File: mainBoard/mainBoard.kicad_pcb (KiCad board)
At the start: 4 copper layers, 110 x 75 mm, 74 parts, among them IC1 TCAN3414DR, J1 XT60PW-M, J10 RJ45, J11 RJ45, J12 Conn_01x03, J16 BM04B-SRSS-TB, J17 BM04B-SRSS-TB, J18 BM04B-SRSS-TB, J19 BM04B-SRSS-TB, J2 XT60PW-M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

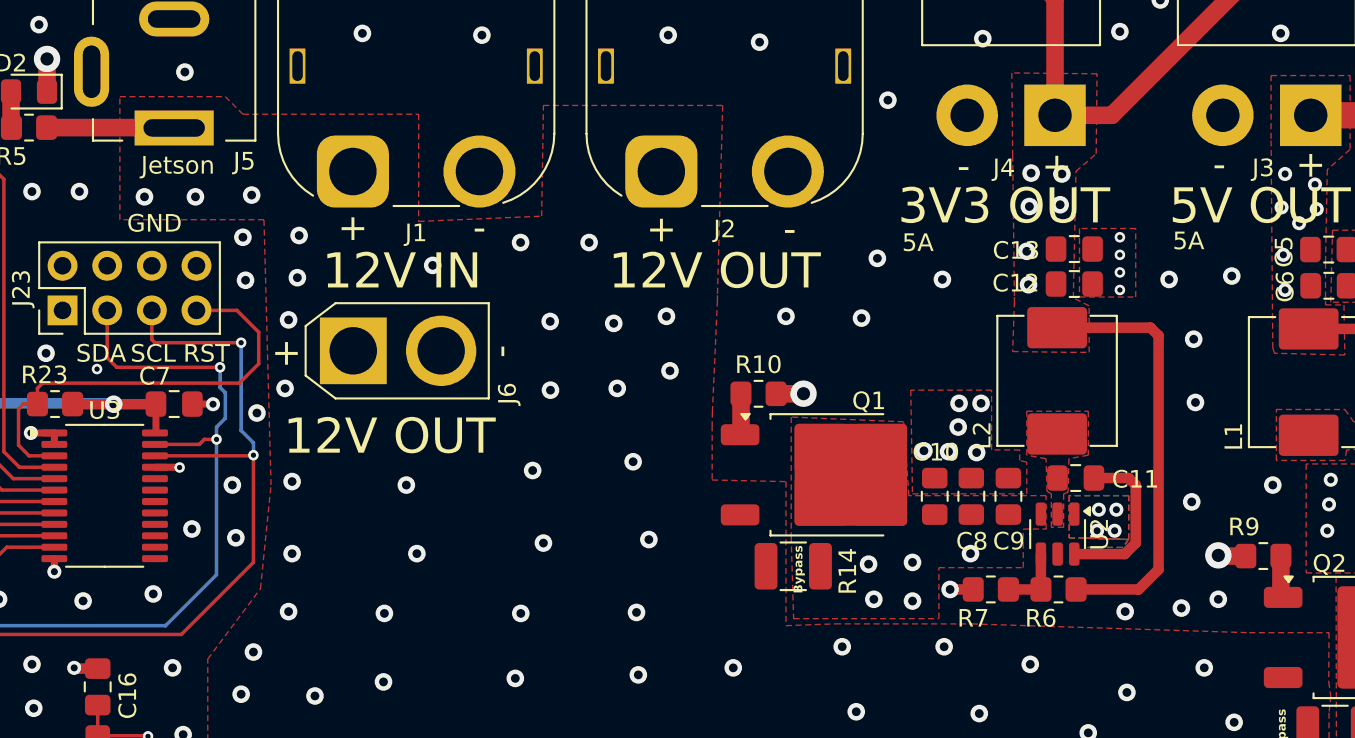
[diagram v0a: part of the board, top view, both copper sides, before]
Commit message: Fixed trace that had a unecessary via
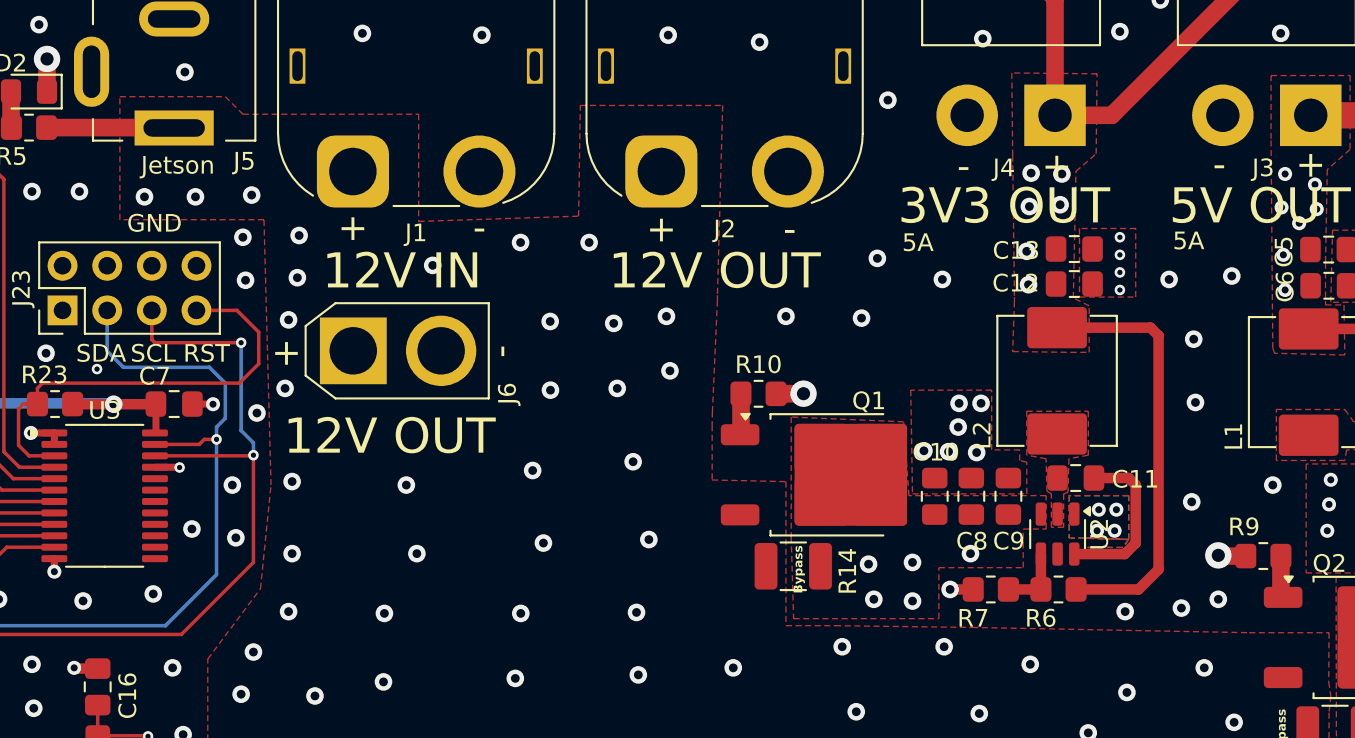
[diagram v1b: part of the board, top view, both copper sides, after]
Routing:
- net SDA1: track 54.6 -> 54.0 mm, vias 3 -> 2
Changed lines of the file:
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@@
 		(tags "resistor handsolder")
 		(property "Reference" "R13"
-			(at 1.1 -2.28 360)
+			(at 1.1 -2.28 0)
 			(layer "F.SilkS")
 			(effects
@@
 		)
 		(property "Value" "0"
-			(at 0 2.28 360)
+			(at 0 2.28 0)
 			(layer "F.Fab")
 			(hide yes)
@@
 		)
 		(fp_text user "${REFERENCE}"
-			(at 0 0 360)
+			(at 0 0 0)
 			(layer "F.Fab")
 			(effects
@@
 		(tags "resistor handsolder")
 		(property "Reference" "R9"
-			(at 1.1 1.65 360)
+			(at 1.1 1.65 0)
 			(layer "F.SilkS")
 			(effects
@@
 		)
 		(property "Value" "100"
-			(at 0 1.65 360)
+			(at 0 1.65 0)
 			(layer "F.Fab")
 			(hide yes)
@@
 		)
 		(fp_text user "${REFERENCE}"
-			(at 0 0 360)
+			(at 0 0 0)
 			(layer "F.Fab")
 			(effects
@@
 	)
 	(segment
-		(start 39.265 47.172643)
-		(end 39.265 44.475)
-		(width 0.2)
-		(layer "F.Cu")
-		(net 22)
-	)
-	(segment
 		(start 45.485786 51.814215)
 		(end 44.785786 51.814215)
@@
 	)
 	(segment
-		(start 45.685786 47.714215)
-		(end 39.806572 47.714215)
-		(width 0.2)
-		(layer "F.Cu")
-		(net 22)
-	)
-	(segment
 		(start 44.785786 51.814215)
 		(end 44.500001 52.1)
@@
 		(net 22)
 	)
-	(segment
-		(start 39.806572 47.714215)
-		(end 39.265 47.172643)
-		(width 0.2)
-		(layer "F.Cu")
-		(net 22)
-	)
 	(via
 		(at 23.385786 68.814215)
@@
 		(net 22)
 	)
-	(via
-		(at 45.685786 47.714215)
-		(size 0.6)
-		(drill 0.3)
-		(layers "F.Cu" "B.Cu")
+	(segment
+		(start 45.985786 48.614215)
+		(end 45.085786 47.714215)
+		(width 0.2)
+		(layer "B.Cu")
 		(net 22)
 	)
 	(segment
-		(start 45.485786 51.114215)
-		(end 45.985786 50.614215)
+		(start 45.085786 47.714215)
+		(end 40.185786 47.714215)
 		(width 0.2)
 		(layer "B.Cu")
@@
 	)
 	(segment
-		(start 45.685786 48.864215)
-		(end 45.685786 47.714215)
+		(start 45.485786 51.814215)
+		(end 45.485786 51.114215)
 		(width 0.2)
 		(layer "B.Cu")
@@
 	)
 	(segment
-		(start 23.385786 66.814215)
-		(end 23.385786 68.814215)
+		(start 40.185786 47.714215)
+		(end 39.265 46.793429)
 		(width 0.2)
 		(layer "B.Cu")
@@
 	)
 	(segment
-		(start 45.485786 51.814215)
-		(end 45.485786 51.114215)
+		(start 45.485786 51.114215)
+		(end 45.985786 50.614215)
 		(width 0.2)
 		(layer "B.Cu")
@@
 	)
 	(segment
-		(start 45.485786 59.514215)
-		(end 42.585786 62.414215)
+		(start 23.385786 66.814215)
+		(end 23.385786 68.814215)
 		(width 0.2)
 		(layer "B.Cu")
@@
 	(segment
 		(start 45.985786 50.614215)
-		(end 45.985786 49.164215)
+		(end 45.985786 48.614215)
+		(width 0.2)
+		(layer "B.Cu")
+		(net 22)
+	)
+	(segment
+		(start 45.485786 59.514215)
+		(end 42.585786 62.414215)
 		(width 0.2)
 		(layer "B.Cu")
@@
 	)
 	(segment
-		(start 45.985786 49.164215)
-		(end 45.685786 48.864215)
+		(start 39.265 46.793429)
+		(end 39.265 44.475)
 		(width 0.2)
 		(layer "B.Cu")
@@
 			(pts
 				(xy 39.985786 32.314215) (xy 45.985786 32.314215) (xy 46.985786 33.314215) (xy 56.985786 33.314215)
-				(xy 56.985786 39.414215) (xy 63.985786 39.114215) (xy 64.085786 32.814215) (xy 74.285786 32.814215)
+				(xy 56.985786 39.414215) (xy 66.085786 39.114215) (xy 66.185786 32.814215) (xy 74.285786 32.814215)
 				(xy 73.985786 43.614215) (xy 73.985786 43.914215) (xy 73.701321 50.22975) (xy 73.685786 51.010643)
-				(xy 73.685786 54.12579) (xy 77.885786 54.216896) (xy 77.885786 62.414215) (xy 80.682821 62.311175)
-				(xy 88.468804 62.314215) (xy 104.24746 62.814215) (xy 108.786664 62.814215) (xy 108.768679 65.614215)
+				(xy 73.685786 54.12579) (xy 77.885786 54.216896) (xy 77.885786 62.414215) (xy 80.682821 62.414215)
+				(xy 88.485786 62.514215) (xy 104.24746 62.814215) (xy 108.786664 62.814215) (xy 108.768679 65.614215)
 				(xy 108.885786 66.414215) (xy 108.785786 67.368271) (xy 108.785786 69.754755) (xy 108.885786 70.214215)
 				(xy 108.914162 70.714215) (xy 108.578295 74.814215) (xy 104.885786 74.814215) (xy 104.885786 79.414215)
@@
 				(xy 113.635786 52.164215) (xy 115.285786 52.214215) (xy 115.285786 52.814215) (xy 115.285786 55.014215)
 				(xy 121.085786 55.014215) (xy 121.085786 56.314215) (xy 121.085786 60.514215) (xy 121.085786 62.714215)
-				(xy 121.085786 62.714215) (xy 121.085786 62.939069)
+				(xy 121.085786 62.939069)
 			)
 		)

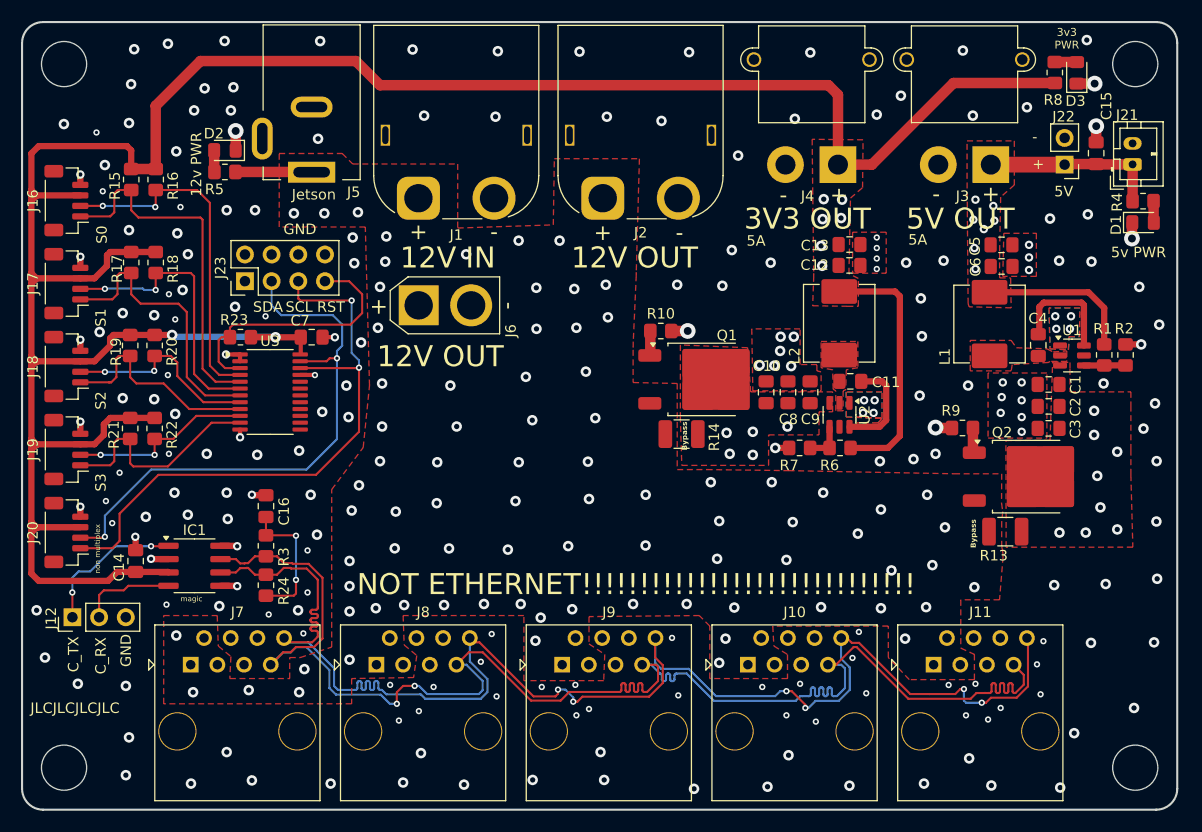
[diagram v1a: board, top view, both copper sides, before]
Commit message: Reviewed PCB with justin and made changes
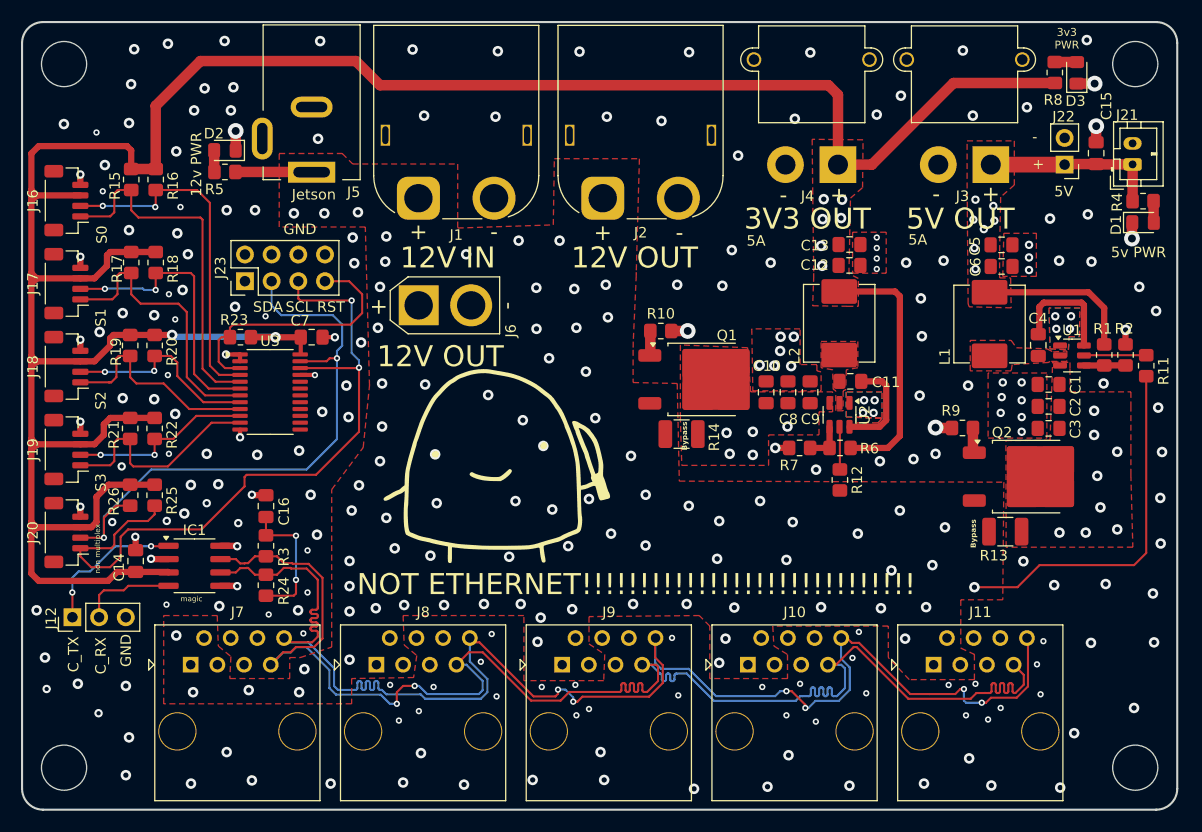
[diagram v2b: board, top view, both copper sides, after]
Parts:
- added G***: LOGO, LOGO, F.Cu at (61.0, 64.1)
- added R11: 10K, Resistor_SMD:R_0805_2012Metric_Pad1.20x1.40mm_HandSolder, F.Cu at (122.5, 52.5)
- added R12: 10K, Resistor_SMD:R_0805_2012Metric_Pad1.20x1.40mm_HandSolder, F.Cu at (93.4, 63.4)
- added R25: 4.7K, Resistor_SMD:R_0805_2012Metric_Pad1.20x1.40mm_HandSolder, F.Cu at (28.1, 64.9)
- added R26: 4.7K, Resistor_SMD:R_0805_2012Metric_Pad1.20x1.40mm_HandSolder, F.Cu at (25.8, 64.9)
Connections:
- U1 pad 5: unconnected-(U1-EN-Pad5) -> Net-(U1-EN)
- U2 pad 5: unconnected-(U2-EN-Pad5) -> Net-(U2-EN)
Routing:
- net +12V: track 7.24 -> 41.8 mm
- net SCL1: track 57.9 -> 69.8 mm
- net +3V3: track 271.7 -> 281.9 mm
- net Net-(U1-EN): track 0.00 -> 5.94 mm
- net SDA1: track 54.0 -> 58.9 mm
- net Net-(U2-EN): track 0.00 -> 4.08 mm
- net GND: track 30.6 -> 30.5 mm, vias 211 -> 215
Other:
- board text removed: "JLCJLCJLCJLC"
